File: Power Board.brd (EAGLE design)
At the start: 13.6 x 28.6 mm, 45 parts, among them IC1 SN74LS00N, Q1 IRLB8743PBF, U1 S18V20F12, U2 D24V22F3, U3 D24V22F5

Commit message: Route PCB
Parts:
- removed R17: 180, resistor:0207/10
- JP2: value Software Killswitch -> Soft Kill
- moved R16 414.5 mm to (-8.89, 106.7)
- moved R12 387.9 mm to (38.1, 114.3)
- moved R15 385.6 mm to (-8.89, 90.2)
- moved R14 384.1 mm to (44.5, 78.7), turned to 90 degrees
- moved R11 371.4 mm to (45.7, 105.4), turned to 90 degrees
- moved R13 369.3 mm to (36.8, 80.0)
- moved R10 346.8 mm to (44.5, 91.4), turned to 90 degrees
- moved R9 340.2 mm to (38.1, 101.6)
- moved D2 114.1 mm to (5.08, 47.0)
- moved D1 103.6 mm to (16.5, 47.0)
- moved R8 94.8 mm to (16.5, 52.1)
- moved R7 78.0 mm to (5.08, 52.1)
- moved R6 77.3 mm to (2.54, 66.0), turned to 90 degrees
- moved R5 63.2 mm to (0.00, 66.0), turned to 270 degrees
- moved MOTOR_PWR 20.4 mm to (5.08, 74.9), flipped to the bottom, turned to 180 degrees
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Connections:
- net N$3 renamed POWER_FET_GATE
- net N$8 renamed LOG_VIN
- net GND: now also R10.1
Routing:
- net +3V3: track 0.00 -> 136.4 mm, vias 0 -> 2
- net VCC: track 0.00 -> 107.4 mm, vias 0 -> 2
- net +12V: track 0.00 -> 107.3 mm, vias 0 -> 4
- net LOG_VIN: track 0.00 -> 64.9 mm
- net MOTOR_0V: track 0.00 -> 55.3 mm, vias 0 -> 2
- net MOTOR_V+: track 0.00 -> 35.1 mm, vias 0 -> 1
- net KILL_SIG: track 0.00 -> 31.7 mm, vias 0 -> 2
- net SOFT_KILL: track 0.00 -> 24.2 mm
- net MOT_VSENS: track 0.00 -> 21.4 mm
- net MOT_BATT_VIN: track 0.00 -> 15.7 mm
- net LOG_VSENS: track 0.00 -> 15.5 mm
- net N$2: track 0.00 -> 12.2 mm
- net N$4: track 0.00 -> 10.7 mm
- net N$7: track 0.00 -> 9.93 mm
- net N$14: track 0.00 -> 9.72 mm, vias 0 -> 1
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- added copper zone on layer 16, net GND
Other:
- board size 13.6 x 28.6 mm -> 64.8 x 91.4 mm
- board text added: "Rev. 1"
- board text added: "USC AUV Power Board"

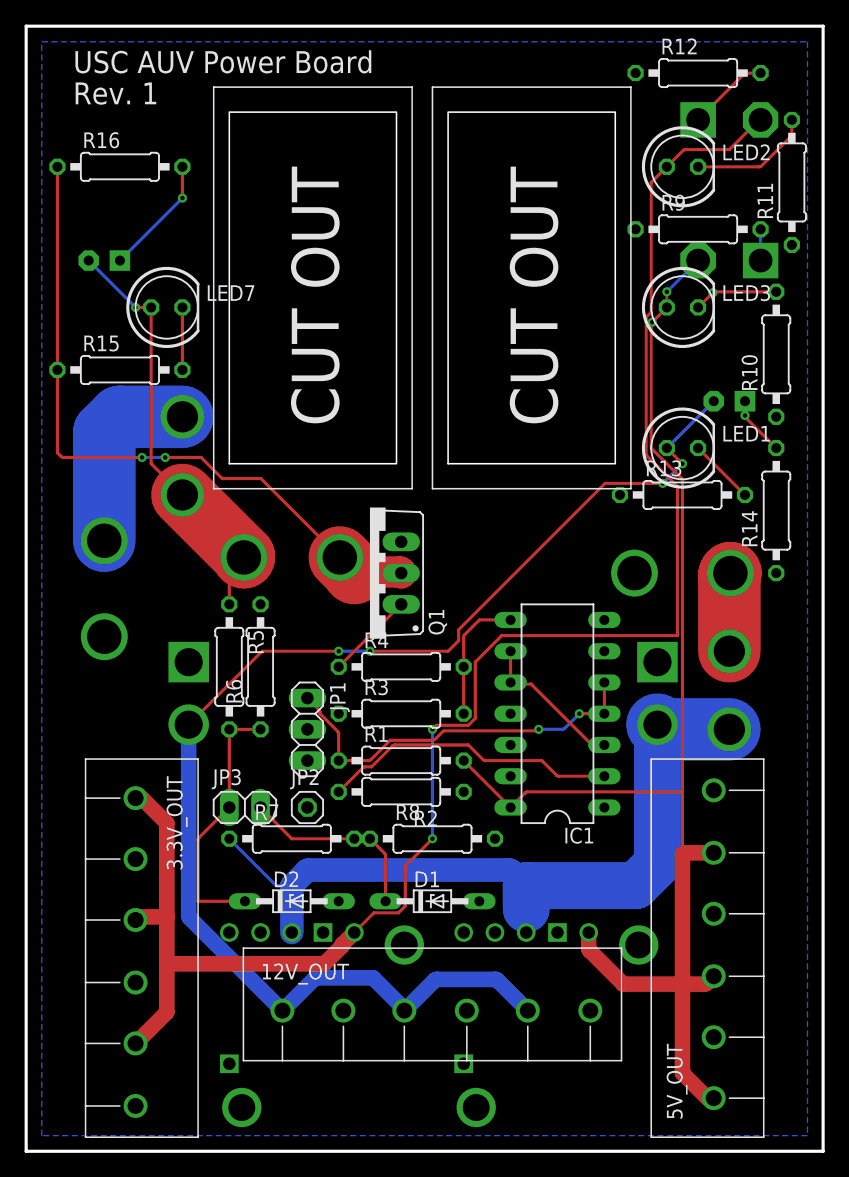
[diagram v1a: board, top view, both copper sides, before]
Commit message: Fix some routing issues for submission to PCB manufacturer
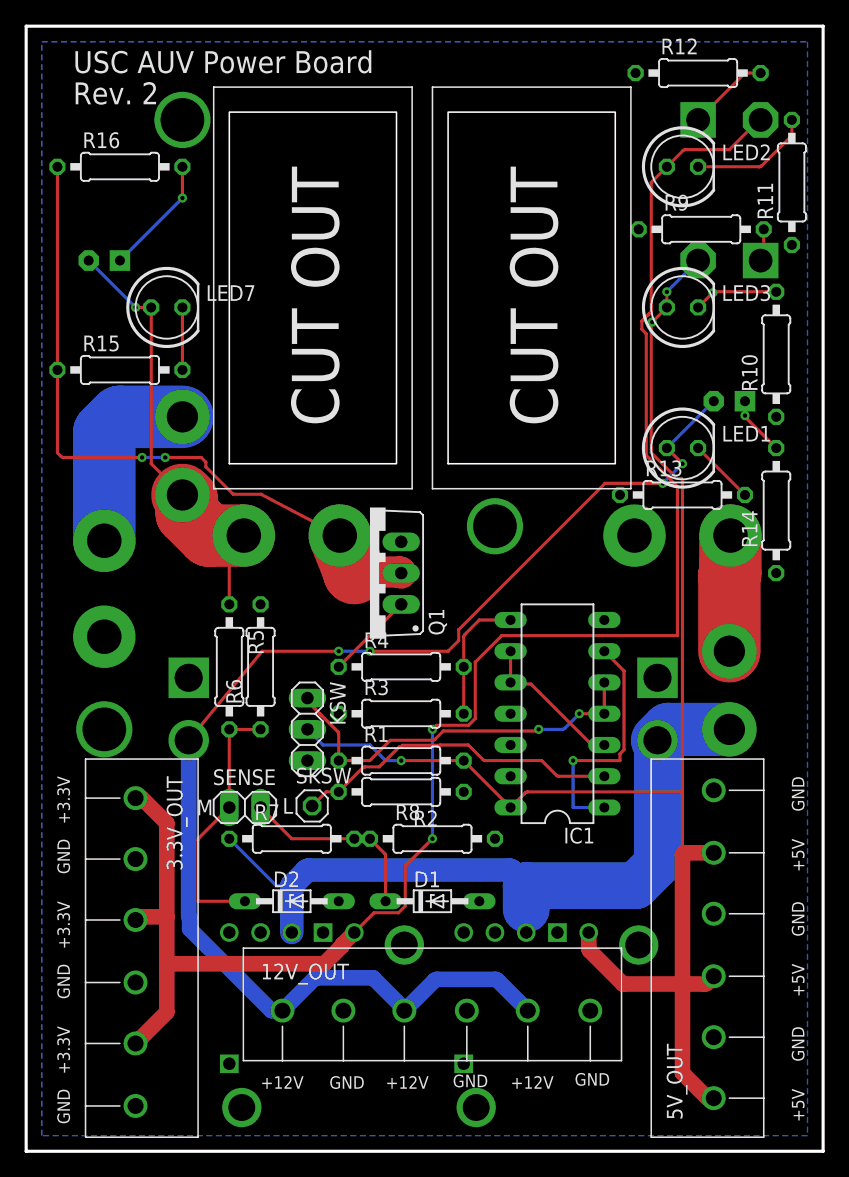
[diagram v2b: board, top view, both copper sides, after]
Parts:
- removed JP2: Soft Kill, pinhead:1X01
- added SKSW: Soft Kill, pinhead:1X01
- moved LOGIC_BATT 3.05 mm to (36.8, 76.7)
- moved MOTOR_PWR 1.78 mm to (5.08, 76.7)
- moved U1 1.27 mm to (15.7, 62.6)
- moved R9 0.25 mm to (38.4, 101.6)
- renumbered JP1 to KSW, JP3 to SENSE
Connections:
- net SOFT_KILL: now also SKSW.1; no longer JP2.1
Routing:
- net N$1: track 0.00 -> 19.8 mm, vias 0 -> 1
- net VCC: track 107.4 -> 121.4 mm, vias 2 -> 3
- net LOG_BATT_VIN: track 6.37 -> 9.41 mm
- net SOFT_KILL: track 24.2 -> 26.8 mm
- net LOG_VIN: track 64.9 -> 63.9 mm
- net MOTOR_V+: track 35.1 -> 35.9 mm
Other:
- board text added: "+12V"
- board text added: "+3.3V"
- board text added: "+5V"
- board text added: "GND"
- board text added: "L"
- board text added: "M"
- board text added: "Rev. 2"
- board text removed: "Rev. 1"

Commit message: Remove large LEDs (they were too hard to find, and produced too much heat)
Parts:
- removed LED4: WHITE_10mm, led:LED10MM
- removed LED5: YEL_10mm, Power Board Custom:SPARKFUN_10MMLED
- removed LED6: RED_10mm, Power Board Custom:SPARKFUN_10MMLED
- removed LED8: BLU_10mm, led:LED10MM
- removed R12: 33, resistor:0207/10
- removed R14: 220, resistor:0207/10
- removed R16: 330, resistor:0207/10
- removed R9: 100, resistor:0207/10
- moved LED7 11.4 mm to (-5.08, 106.7)
- moved R15 6.84 mm to (-6.35, 96.5), turned to 90 degrees
- moved R11 1.27 mm to (45.7, 104.1)
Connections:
- removed net N$11: LED4.K, R14.2
- removed net N$14: LED8.K, R16.2
- removed net N$5: LED6.K, R9.2
- removed net N$9: LED5.K, R12.2
- net +12V: no longer LED4.A
- net +3V3: no longer LED5.A
- net GND: no longer R12.1, R14.1, R9.1
- net MOTOR_0V: no longer R16.1
- net MOTOR_V+: no longer LED8.A
- net VCC: no longer LED6.A
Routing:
- net MOTOR_0V: track 55.7 -> 32.5 mm, vias 2 -> 1
- net N$14: track 9.72 -> 0.00 mm, vias 1 -> 0
- net +3V3: track 136.7 -> 127.6 mm
- net MOTOR_V+: track 35.9 -> 42.8 mm, vias 1 -> 0
- net N$9: track 6.64 -> 0.00 mm
- net +12V: track 107.5 -> 102.1 mm
- net N$13: track 5.08 -> 0.00 mm
- net N$11: track 4.85 -> 0.00 mm, vias 1 -> 0
- net VCC: track 121.4 -> 117.8 mm
- net N$5: track 2.65 -> 0.00 mm
- net N$7: track 9.93 -> 8.66 mm
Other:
- board text added: "Rev. 3"
- board text removed: "Rev. 2"

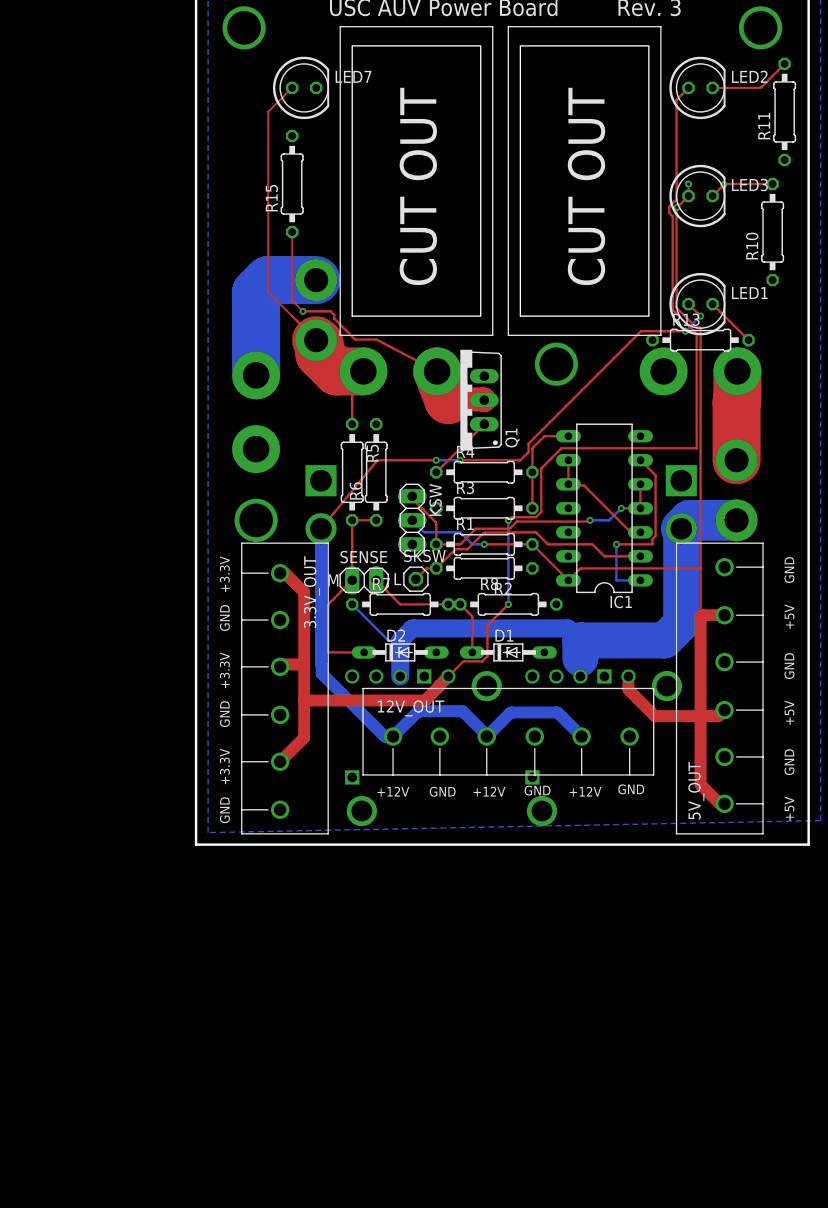
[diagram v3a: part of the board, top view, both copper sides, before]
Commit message: Start on new SMD version of power board -- add LTC FET driver, convert NAND gate to SMD
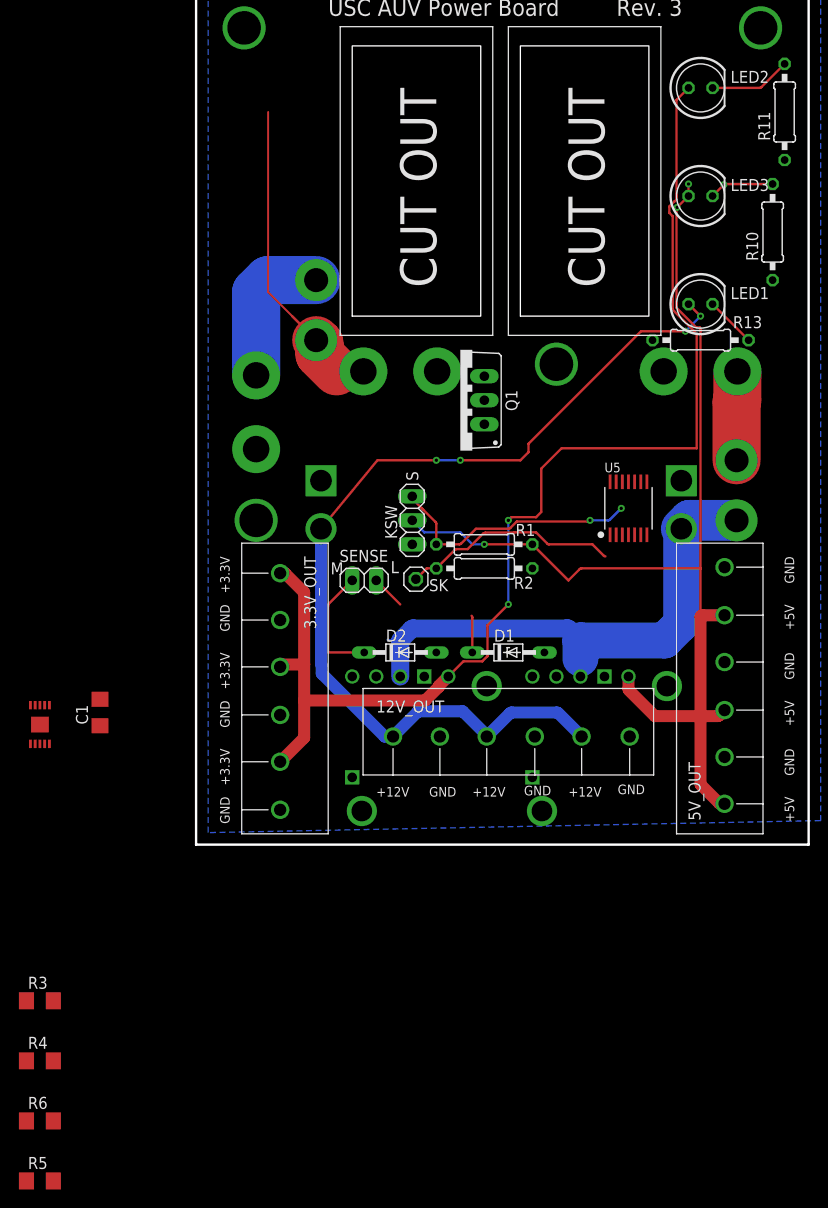
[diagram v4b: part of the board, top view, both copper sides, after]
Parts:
- removed IC1: SN74LS00N, 74xx-us:DIL14
- removed LED7: BLU, led:LED5MM
- removed R15: 1K, resistor:0207/10
- removed R7: 22K, resistor:0207/10
- removed R8: 3.3K, resistor:0207/10
- added C1: .1uF, rcl:C1206
- added U4: LTC7004, Power Board Custom:10-MSOP
- added U5: CD4011BPWR, Power Board Custom:14-TSSOP
- R3: value 10K -> 3.3K; device resistor:0207/10 -> rcl:R1206
- R4: value 220 -> 3.3K; device resistor:0207/10 -> rcl:R1206
- R5: value 22K -> 3.3K; device resistor:0207/10 -> rcl:R1206
- R6: value 3.3K -> 22K; device resistor:0207/10 -> rcl:R1206
- moved R5 81.9 mm to (-33.0, -8.89), turned to 0 degrees
- moved R4 78.0 mm to (-33.0, 3.81)
- moved R6 77.3 mm to (-33.0, -2.54), turned to 0 degrees
- moved R3 70.1 mm to (-33.0, 10.2)
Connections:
- removed net MOTOR_0V: MOTOR_PWR.BLACK, Q1.D, R15.1
- removed net N$1: IC1.1, IC1.6
- removed net N$13: LED7.K, R15.2
- removed net POWER_FET_GATE: Q1.G, R4.1
- new net N$11: C1.1, U4.P9
- new net N$3: U5.P4, U5.P8, U5.P9
- new net N$8: Q1.G, U4.P6, U4.P7
- new net N$9: C1.2, MOTOR_PWR.RED, Q1.S, U4.P8
- net +3V3: now also U5.P14
- net GND: now also MOTOR_PWR.BLACK, R4.1, U4.BOTTOM, U4.P2, U4.P3, U4.P5, U5.P12, U5.P13, U5.P7; no longer IC1.12, IC1.13, IC1.7, Q1.S, R6.2, R8.2
- net KILL_SIG: now also U5.P1, U5.P2; no longer IC1.4, IC1.5
- net LOG_VIN: now also R6.2; no longer R7.1
- net LOG_VSENS: now also R4.2, R6.1; no longer R7.2, R8.1
- net MOTOR_V+: now also Q1.D, R5.2; no longer LED7.A, MOTOR_PWR.RED, R5.1
- net MOT_VSENS: now also R3.2, R5.1; no longer R5.2, R6.1
- net N$2: now also U5.P3, U5.P5; no longer IC1.10, IC1.3, IC1.9
- net N$4: now also U4.P4, U5.P10; no longer IC1.8, R3.2, R4.2
- net SOFT_KILL: now also U5.P6; no longer IC1.2
- net VCC: now also U4.P1; no longer IC1.14
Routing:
- net MOTOR_0V: track 32.5 -> 0.00 mm, vias 1 -> 0
- net N$1: track 19.8 -> 0.00 mm, vias 1 -> 0
- net MOTOR_V+: track 42.8 -> 30.4 mm
- net N$2: track 12.2 -> 0.00 mm
- net N$4: track 10.7 -> 0.00 mm
- net MOT_VSENS: track 21.4 -> 12.5 mm
- net LOG_VSENS: track 15.5 -> 7.49 mm
- net POWER_FET_GATE: track 7.18 -> 0.00 mm
- net LOG_VIN: track 63.9 -> 58.6 mm
- net KILL_SIG: track 31.9 -> 27.2 mm
- net SOFT_KILL: track 26.8 -> 23.1 mm
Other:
- board text added: "S"
- board text added: "SK"

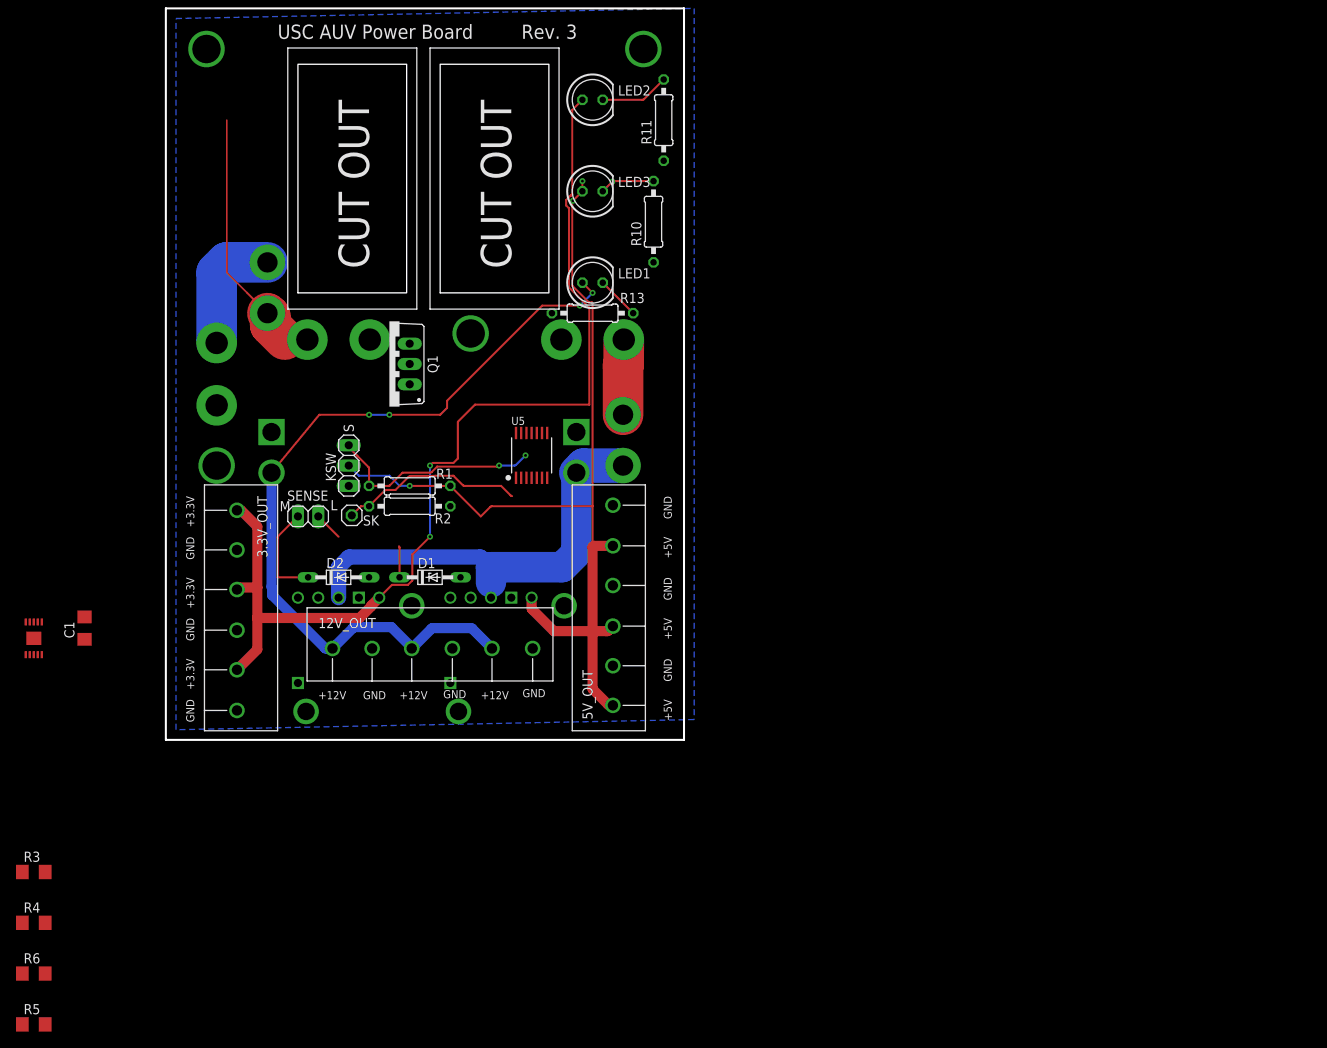
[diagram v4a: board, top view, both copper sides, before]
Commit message: Switch LEDs to surface mount, add LTC MOSFET driver
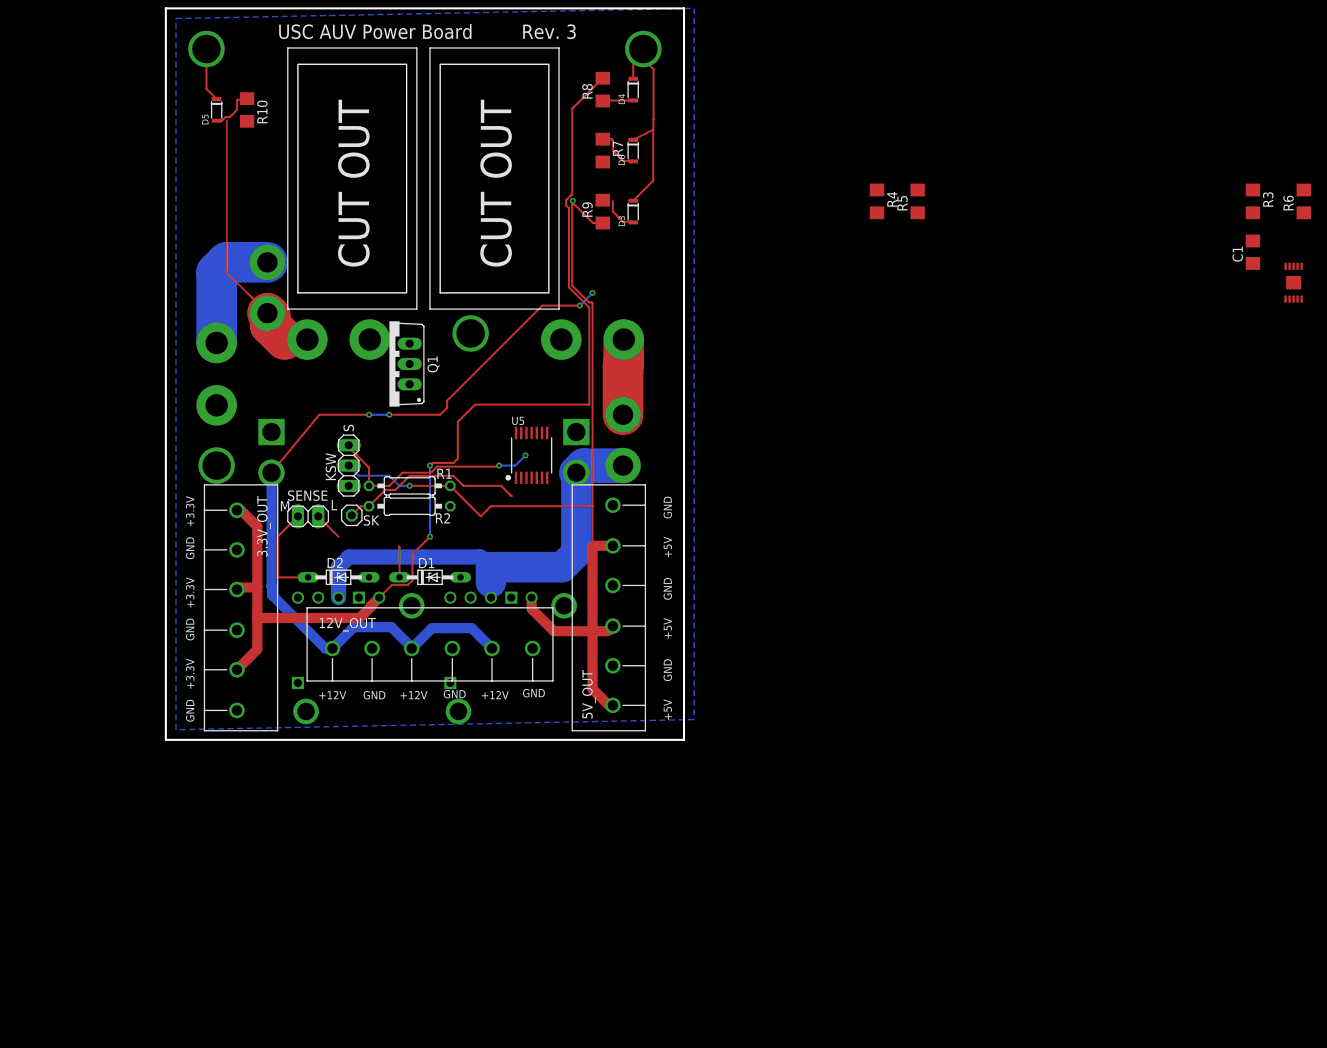
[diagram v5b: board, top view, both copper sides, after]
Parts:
- removed LED1: (no value), led:LED5MM
- removed LED2: YEL, led:LED5MM
- removed LED3: RED, led:LED5MM
- removed R11: 100, resistor:0207/10
- removed R13: 1K, resistor:0207/10
- added D3: LTST-C150KRKT, Power Board Custom:LITEON_LED_1206
- added D4: LTST-C150KSKT, Power Board Custom:LITEON_LED_1206
- added D5: LTST-C150TBKT, Power Board Custom:LITEON_LED_1206
- added D6: LTW-150TK, Power Board Custom:LITEON_LED_1206
- added R7: 470, rcl:R1206
- added R8: 130, rcl:R1206
- added R9: 200, rcl:R1206
- R10: value 180 -> 800; device resistor:0207/10 -> rcl:R1206
- moved R6 185.8 mm to (125.7, 94.0), turned to 90 degrees
- moved R3 173.9 mm to (119.4, 94.0), turned to 270 degrees
- moved U4 163.6 mm to (124.5, 83.8), turned to 180 degrees
- moved C1 153.4 mm to (119.4, 87.6)
- moved R5 151.0 mm to (77.5, 94.0), turned to 90 degrees
- moved R4 138.7 mm to (72.4, 94.0), turned to 270 degrees
- moved R10 52.7 mm to (-6.35, 105.4), turned to 270 degrees
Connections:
- removed net N$10: LED1.K, R13.2
- new net N$1: D6.A, R7.1
- new net N$5: D4.A, R8.1
- net +12V: now also R7.2; no longer LED1.A
- net +3V3: now also R8.2; no longer LED2.A
- net GND: now also D3.C, D4.C, D5.C, D6.C; no longer R10.1, R11.1, R13.1
- net N$6: now also D3.A, R9.1; no longer LED3.K, R10.2
- net N$7: now also D5.A, R10.1; no longer LED2.K, R11.2
- net N$9: now also R10.2
- net VCC: now also R9.2; no longer LED3.A
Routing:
- net GND: track 0.00 -> 34.4 mm
- net N$1: track 0.00 -> 5.70 mm
- net N$10: track 5.39 -> 0.00 mm
- net N$5: track 0.00 -> 3.84 mm
- net +3V3: track 127.6 -> 131.3 mm
- net N$7: track 8.66 -> 5.70 mm
- net N$6: track 6.86 -> 4.37 mm, vias 1 -> 0
- net VCC: track 117.8 -> 119.7 mm, vias 3 -> 2
- net +12V: track 102.1 -> 100.3 mm
